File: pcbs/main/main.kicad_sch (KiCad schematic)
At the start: 17 parts

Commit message: Switch from RJ11 to screw terminals for power
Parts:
- removed J?: RJ11, symbol Connector:RJ11
- added J?: Screw_Terminal_01x02, TerminalBlock:TerminalBlock_bornier-2_P5.08mm, symbol Connector:Screw_Terminal_01x02
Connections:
- net +12V: now also J?.1 (Pin_1)
- net at F?.1: now also J?.2 (Pin_2)
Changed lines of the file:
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@@
     (stroke (width 0) (type default) (color 0 0 0 0))
   )
-  (wire (pts (xy 43.18 33.02) (xy 41.91 33.02))
+  (wire (pts (xy 33.02 33.02) (xy 43.18 33.02))
     (stroke (width 0) (type default) (color 0 0 0 0))
   )
@@
     (stroke (width 0) (type default) (color 0 0 0 0))
   )
-  (wire (pts (xy 41.91 35.56) (xy 44.45 35.56))
+  (wire (pts (xy 33.02 35.56) (xy 44.45 35.56))
     (stroke (width 0) (type default) (color 0 0 0 0))
   )
@@
     )
     (pin "1")
+  )
+  (symbol (lib_id "Connector:Screw_Terminal_01x02") (at 27.94 35.56 180) (unit 1)
+    (in_bom yes) (on_board yes) (fields_autoplaced)
+    (property "Reference" "J?" (id 0) (at 27.94 26.67 0))
+    (property "Value" "Screw_Terminal_01x02" (id 1) (at 27.94 29.21 0))
+    (property "Footprint" "TerminalBlock:TerminalBlock_bornier-2_P5.08mm" (id 2) (at 27.94 35.56 0)
+      (effects (font (size 1.27 1.27)) hide)
+    )
+    (property "Datasheet" "~" (id 3) (at 27.94 35.56 0)
+      (effects (font (size 1.27 1.27)) hide)
+    )
+    (pin "1")
+    (pin "2")
   )
   (symbol (lib_id "power:GND") (at 99.06 41.91 0) (unit 1)
@@
     (pin "5")
   )
-  (symbol (lib_id "Connector:RJ11") (at 31.75 35.56 0) (unit 1)
-    (in_bom yes) (on_board yes) (fields_autoplaced)
-    (property "Reference" "J?" (id 0) (at 31.75 20.32 0))
-    (property "Value" "RJ11" (id 1) (at 31.75 22.86 0))
-    (property "Footprint" "" (id 2) (at 31.75 34.925 90)
-      (effects (font (size 1.27 1.27)) hide)
-    )
-    (property "Datasheet" "~" (id 3) (at 31.75 34.925 90)
-      (effects (font (size 1.27 1.27)) hide)
-    )
-    (pin "1")
-    (pin "2")
-  )
   (sheet (at 250.19 128.27) (size 31.75 12.7) (fields_autoplaced)
     (stroke (width 0.1524) (type solid) (color 0 0 0 0))
@@
       (reference "J?") (unit 1) (value "Conn_01x08") (footprint "")
     )
+    (path "/457227dc-56a2-4735-a1a8-602fed6c312a"
+      (reference "J?") (unit 1) (value "Screw_Terminal_01x02") (footprint "TerminalBlock:TerminalBlock_bornier-2_P5.08mm")
+    )
     (path "/62451b51-17ea-4233-b63c-77d1085c6d76"
       (reference "J?") (unit 1) (value "Conn_01x05") (footprint "")
@@
       (reference "J?") (unit 1) (value "Conn_01x05") (footprint "")
     )
-    (path "/ff486bb2-aeb3-4ab3-ab41-322fb9146bd7"
-      (reference "J?") (unit 1) (value "RJ11") (footprint "")
-    )
     (path "/7163505d-16c1-4f6c-b99a-5380cb6bb872"

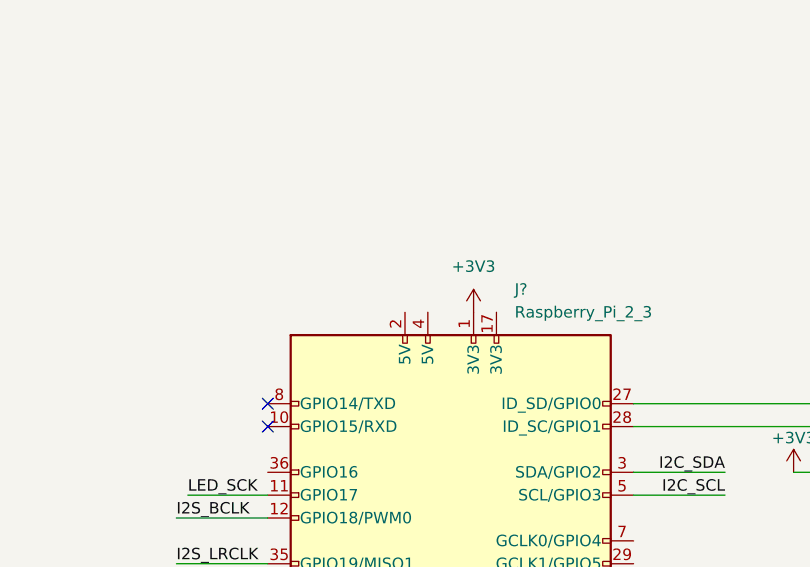
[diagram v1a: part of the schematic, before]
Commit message: Connect Pi to +5V
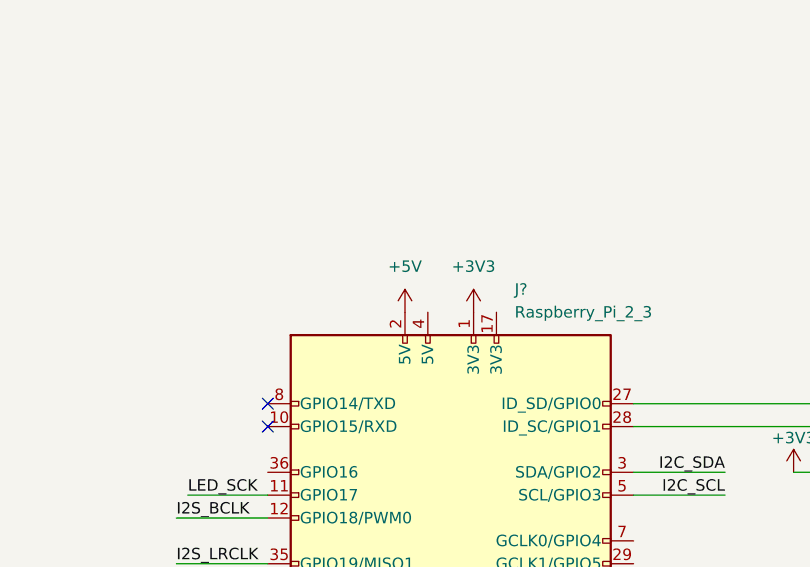
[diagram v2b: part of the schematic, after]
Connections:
- net +5V: now also J?.2 (5V)
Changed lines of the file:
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@@
     (pin "8")
+  )
+  (symbol (lib_id "power:+5V") (at 62.23 83.82 0) (unit 1)
+    (in_bom yes) (on_board yes) (fields_autoplaced)
+    (property "Reference" "#PWR?" (id 0) (at 62.23 87.63 0)
+      (effects (font (size 1.27 1.27)) hide)
+    )
+    (property "Value" "+5V" (id 1) (at 62.23 78.74 0))
+    (property "Footprint" "" (id 2) (at 62.23 83.82 0)
+      (effects (font (size 1.27 1.27)) hide)
+    )
+    (property "Datasheet" "" (id 3) (at 62.23 83.82 0)
+      (effects (font (size 1.27 1.27)) hide)
+    )
+    (pin "1")
   )
   (symbol (lib_id "Device:R") (at 111.76 101.6 90) (unit 1)
@@
       (reference "#PWR?") (unit 1) (value "+3V3") (footprint "")
     )
+    (path "/37d9499b-fbe0-44df-957d-295cd162b1cf"
+      (reference "#PWR?") (unit 1) (value "+5V") (footprint "")
+    )
     (path "/c9bcbb20-bce5-48eb-aaa8-469331798139/3c2d9b15-6e23-49f8-88ff-b6df4c03ecd8"
